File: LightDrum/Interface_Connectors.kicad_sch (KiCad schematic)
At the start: 3 parts, among them J1201 0525593652, J1202 0541323662, J1203 PWR-CONN

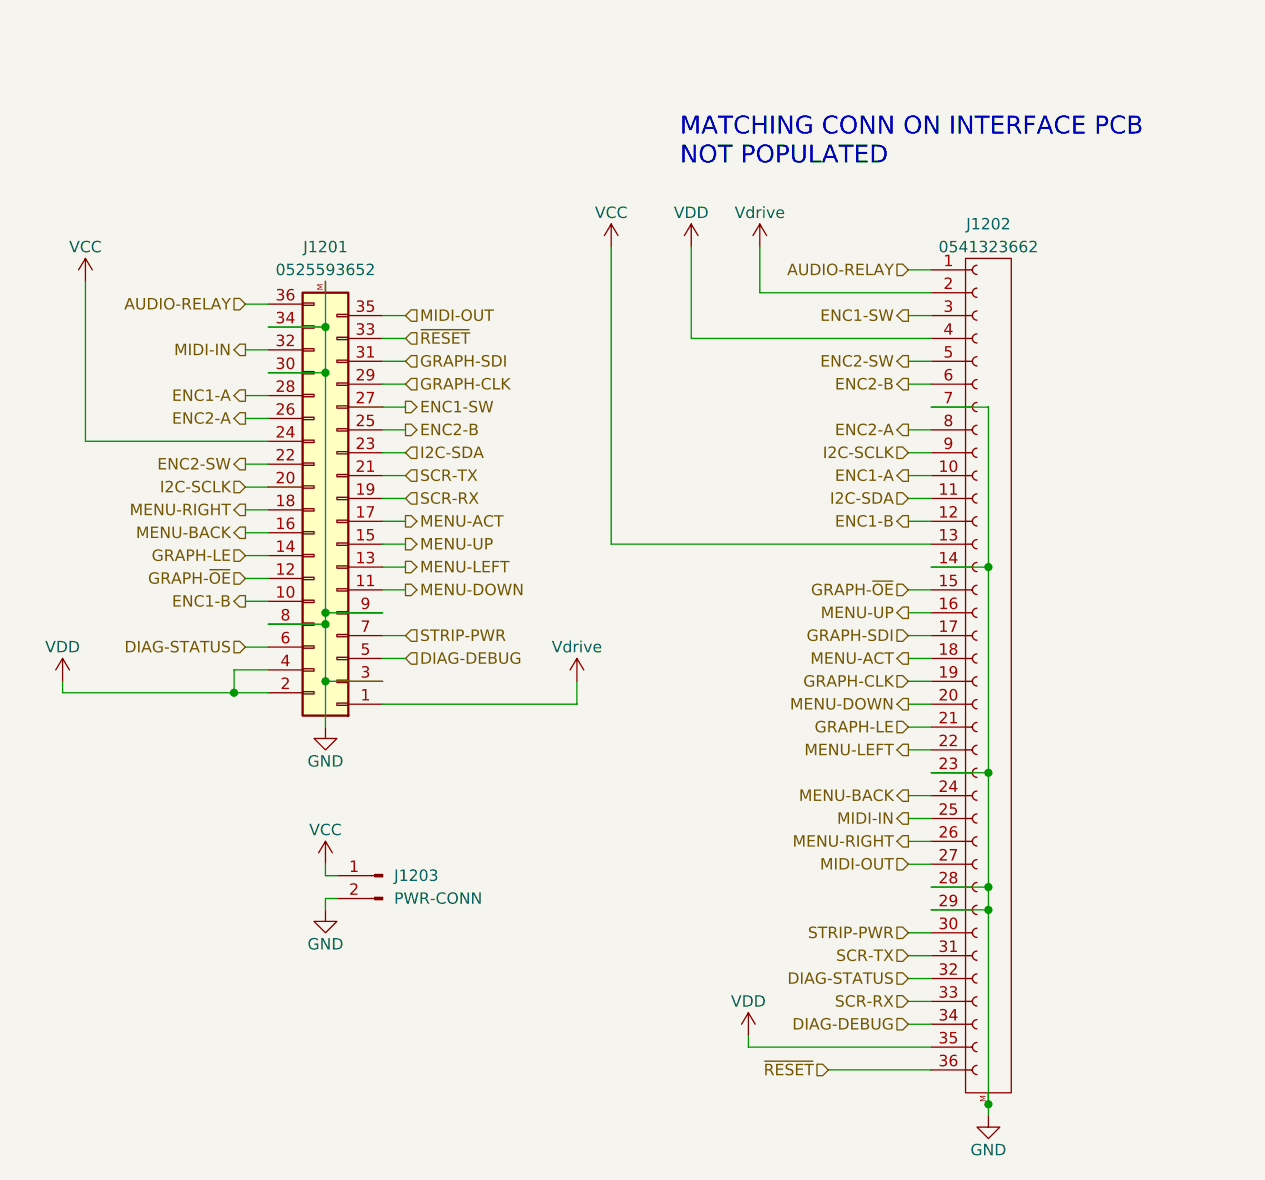
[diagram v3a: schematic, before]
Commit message: Replace MCU finished. REV9
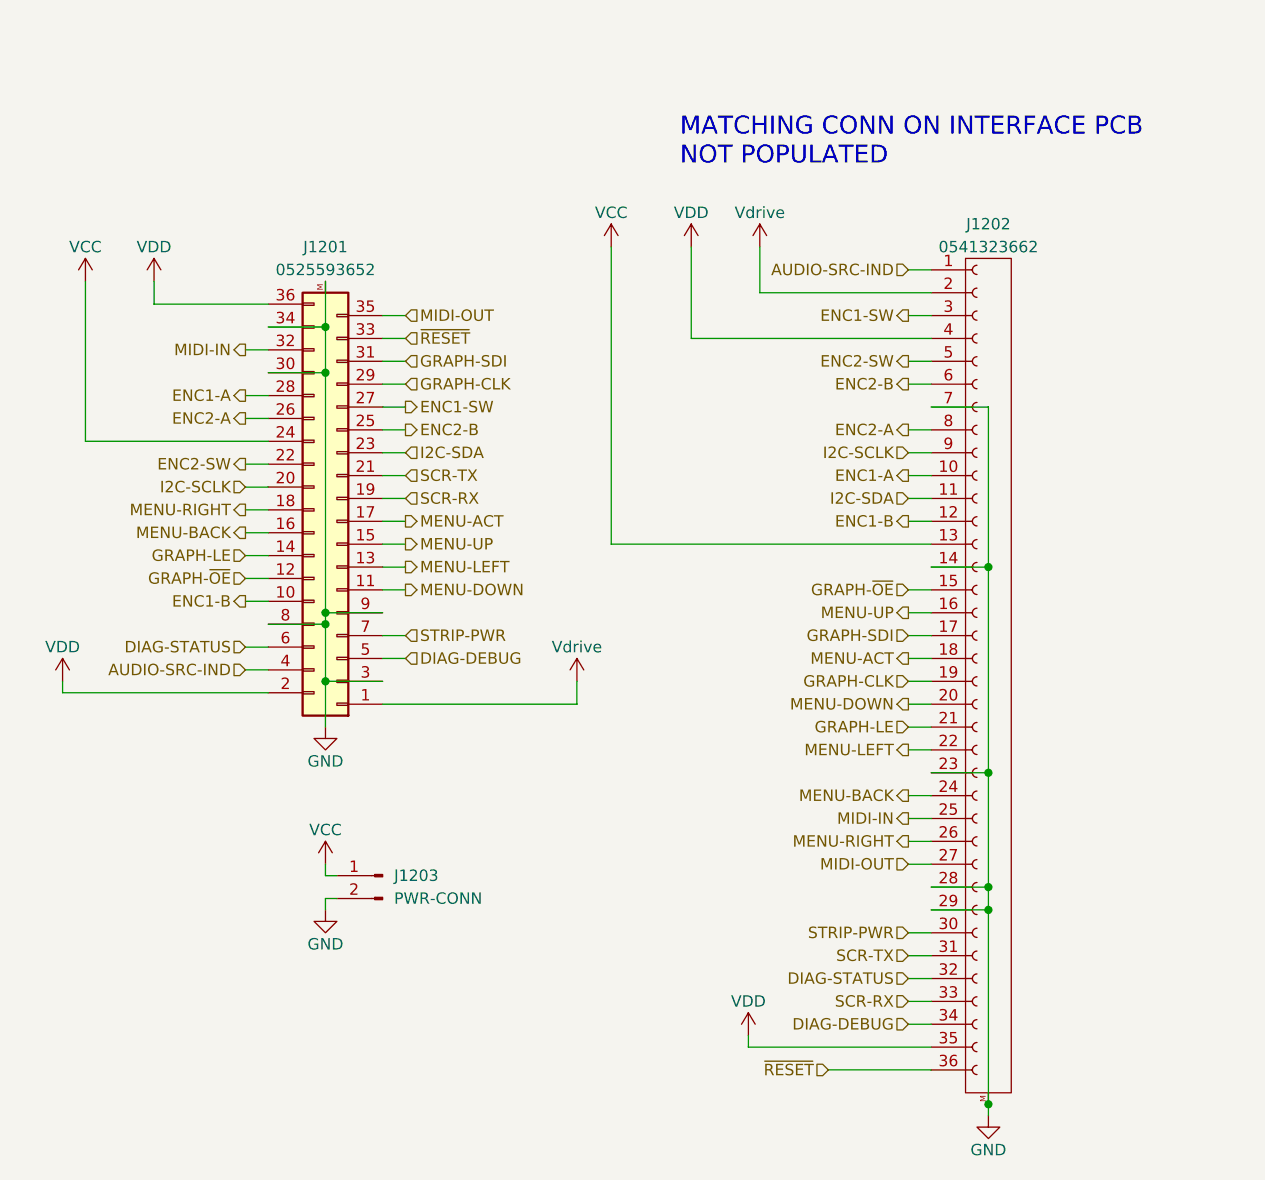
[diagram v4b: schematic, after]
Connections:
- net VDD: now also J1201.36 (Pin_36); no longer J1201.4 (Pin_4)
- net AUDIO-RELAY renamed AUDIO-SRC-IND
- net AUDIO-SRC-IND: now also J1201.4 (Pin_4); no longer J1201.36 (Pin_36)
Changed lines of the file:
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@@
   (title_block
     (title "LightDrum")
-    (rev "REV8")
+    (rev "REV9")
     (company "Daxxn Industries")
   )
   (junction (at 124.46 99.06) (diameter 0) (color 0 0 0 0)
   )
-  (junction (at 40.64 90.17) (diameter 0) (color 0 0 0 0)
-  )
   (junction (at 124.46 111.76) (diameter 0) (color 0 0 0 0)
   )
@@
     (stroke (width 0) (type default) (color 0 0 0 0))
   )
-  (wire (pts (xy 40.64 90.17) (xy 44.45 90.17))
+  (wire (pts (xy 21.59 90.17) (xy 44.45 90.17))
     (stroke (width 0) (type default) (color 0 0 0 0))
   )
@@
     (stroke (width 0) (type default) (color 0 0 0 0))
   )
-  (wire (pts (xy 21.59 90.17) (xy 40.64 90.17))
-    (stroke (width 0) (type default) (color 0 0 0 0))
-  )
   (wire (pts (xy 118.11 76.2) (xy 124.46 76.2))
     (stroke (width 0) (type default) (color 0 0 0 0))
@@
     (stroke (width 0) (type default) (color 0 0 0 0))
   )
-  (wire (pts (xy 40.64 87.63) (xy 40.64 90.17))
-    (stroke (width 0) (type default) (color 0 0 0 0))
-  )
   (wire (pts (xy 118.11 99.06) (xy 124.46 99.06))
     (stroke (width 0) (type default) (color 0 0 0 0))
@@
     (stroke (width 0) (type default) (color 0 0 0 0))
   )
+  (wire (pts (xy 44.45 46.99) (xy 31.75 46.99))
+    (stroke (width 0) (type default) (color 0 0 0 0))
+  )
   (wire (pts (xy 41.91 72.39) (xy 44.45 72.39))
     (stroke (width 0) (type default) (color 0 0 0 0))
@@
     (stroke (width 0) (type default) (color 0 0 0 0))
   )
-  (wire (pts (xy 40.64 87.63) (xy 44.45 87.63))
-    (stroke (width 0) (type default) (color 0 0 0 0))
-  )
   (wire (pts (xy 118.11 104.14) (xy 115.57 104.14))
     (stroke (width 0) (type default) (color 0 0 0 0))
@@
     (stroke (width 0) (type default) (color 0 0 0 0))
   )
+  (wire (pts (xy 31.75 44.45) (xy 31.75 46.99))
+    (stroke (width 0) (type default) (color 0 0 0 0))
+  )
   (wire (pts (xy 41.91 69.85) (xy 44.45 69.85))
     (stroke (width 0) (type default) (color 0 0 0 0))
@@
     (stroke (width 0) (type default) (color 0 0 0 0))
   )
-  (wire (pts (xy 41.91 46.99) (xy 44.45 46.99))
+  (wire (pts (xy 41.91 87.63) (xy 44.45 87.63))
     (stroke (width 0) (type default) (color 0 0 0 0))
   )
@@
     (effects (font (size 2 2)) (justify left bottom))
   )
-  (hierarchical_label "AUDIO-RELAY" (shape input) (at 115.57 43.18 180)
+  (hierarchical_label "AUDIO-SRC-IND" (shape input) (at 115.57 43.18 180)
     (effects (font (size 1.27 1.27)) (justify right))
   )
@@
     (effects (font (size 1.27 1.27)) (justify right))
   )
-  (hierarchical_label "AUDIO-RELAY" (shape input) (at 41.91 46.99 180)
+  (hierarchical_label "AUDIO-SRC-IND" (shape input) (at 41.91 87.63 180)
     (effects (font (size 1.27 1.27)) (justify right))
   )
@@
     (effects (font (size 1.27 1.27)) (justify right))
   )
+  (symbol (lib_id "power:VDD") (at 31.75 44.45 0) (unit 1)
+    (in_bom yes) (on_board yes)
+    (property "Reference" "#PWR0143" (id 0) (at 31.75 48.26 0)
+      (effects (font (size 1.27 1.27)) hide)
+    )
+    (property "Value" "VDD" (id 1) (at 31.75 40.64 0))
+    (property "Footprint" "" (id 2) (at 31.75 44.45 0)
+      (effects (font (size 1.27 1.27)) hide)
+    )
+    (property "Datasheet" "" (id 3) (at 31.75 44.45 0)
+      (effects (font (size 1.27 1.27)) hide)
+    )
+    (pin "1")
+  )
   (symbol (lib_id "power:GND") (at 50.8 93.98 0) (unit 1)

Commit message: interface layout completed - REV6
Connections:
- net AUDIO-SRC-IND: now also J1202.33 (Pin_33); no longer J1202.1 (Pin_1)
- net DIAG-DEBUG: now also J1202.32 (Pin_32); no longer J1202.34 (Pin_34)
- net DIAG-STATUS: now also J1202.31 (Pin_31); no longer J1202.32 (Pin_32)
- net ENC1-A: now also J1202.9 (Pin_9); no longer J1202.10 (Pin_10)
- net ENC1-B: now also J1202.27 (Pin_27); no longer J1202.12 (Pin_12)
- net ENC1-SW: now also J1202.10 (Pin_10); no longer J1202.3 (Pin_3)
- net ENC2-A: now also J1202.11 (Pin_11); no longer J1202.8 (Pin_8)
- net ENC2-B: now also J1202.12 (Pin_12); no longer J1202.6 (Pin_6)
- net ENC2-SW: now also J1202.15 (Pin_15); no longer J1202.5 (Pin_5)
- net GND: now also J1202.3 (Pin_3), J1202.34 (Pin_34); no longer J1202.14 (Pin_14), J1202.23 (Pin_23)
- net GRAPH-CLK: now also J1202.8 (Pin_8); no longer J1202.19 (Pin_19)
- net GRAPH-LE: now also J1202.23 (Pin_23); no longer J1202.21 (Pin_21)
- net GRAPH-SDI: now also J1202.6 (Pin_6); no longer J1202.17 (Pin_17)
- net GRAPH-~{OE}: now also J1202.25 (Pin_25); no longer J1202.15 (Pin_15)
- net I2C-SCLK: now also J1202.17 (Pin_17); no longer J1202.9 (Pin_9)
- net I2C-SDA: now also J1202.14 (Pin_14); no longer J1202.11 (Pin_11)
- net MENU-ACT: now also J1202.20 (Pin_20); no longer J1202.18 (Pin_18)
- net MENU-BACK: now also J1202.21 (Pin_21); no longer J1202.24 (Pin_24)
- net MENU-DOWN: now also J1202.26 (Pin_26); no longer J1202.20 (Pin_20)
- net MENU-LEFT: now also J1202.24 (Pin_24); no longer J1202.22 (Pin_22)
- net MENU-RIGHT: now also J1202.19 (Pin_19); no longer J1202.26 (Pin_26)
- net MENU-UP: now also J1202.22 (Pin_22); no longer J1202.16 (Pin_16)
- net MIDI-IN: now also J1202.5 (Pin_5); no longer J1202.25 (Pin_25)
- net MIDI-OUT: now also J1202.2 (Pin_2); no longer J1202.27 (Pin_27)
- net SCR-RX: now also J1202.18 (Pin_18); no longer J1202.33 (Pin_33)
- net SCR-TX: now also J1202.16 (Pin_16); no longer J1202.31 (Pin_31)
- net VDD: now also J1202.1 (Pin_1); no longer J1202.4 (Pin_4)
- net Vdrive: now also J1202.36 (Pin_36); no longer J1202.2 (Pin_2)
- net ~{RESET}: now also J1202.4 (Pin_4); no longer J1202.36 (Pin_36)
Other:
- note added: "1"
- note added: "10"
- note added: "11"
- note added: "12"
- note added: "13"
- note added: "14"
- note added: "15"
- note added: "16"
- note added: "17"
- note added: "18"
- note added: "19"
- note added: "2"
- note added: "20"
- note added: "21"
- note added: "22"
- note added: "23"
- note added: "24"
- note added: "25"
- note added: "26"
- note added: "27"
- note added: "28"
- note added: "29"
- note added: "3"
- note added: "30"
- note added: "31"
- note added: "32"
- note added: "33"
- note added: "34"
- note added: "35"
- note added: "36"
- note added: "4"
- note added: "5"
- note added: "6"
- note added: "7"
- note added: "8"
- note added: "9"
